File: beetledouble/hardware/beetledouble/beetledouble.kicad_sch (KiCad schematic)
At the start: 29 parts, among them J1 XT30PW-M, J2 rxin, J6 prog connector, U1 78L12G-AB3-R, U2 DD4012SB, U3 ATtiny1614-SS

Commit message: update pcb
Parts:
- added C?: 2.2uF 50V, Capacitor_SMD:C_0603_1608Metric, symbol Device:C
- added C?: 10uF 50V, Capacitor_SMD:C_1206_3216Metric, symbol Device:C
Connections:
- net +12V: now also C?.1, C?.1
- net GND: now also C?.2, C?.2
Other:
- moved on the sheet: C1, C2, TP1, U1

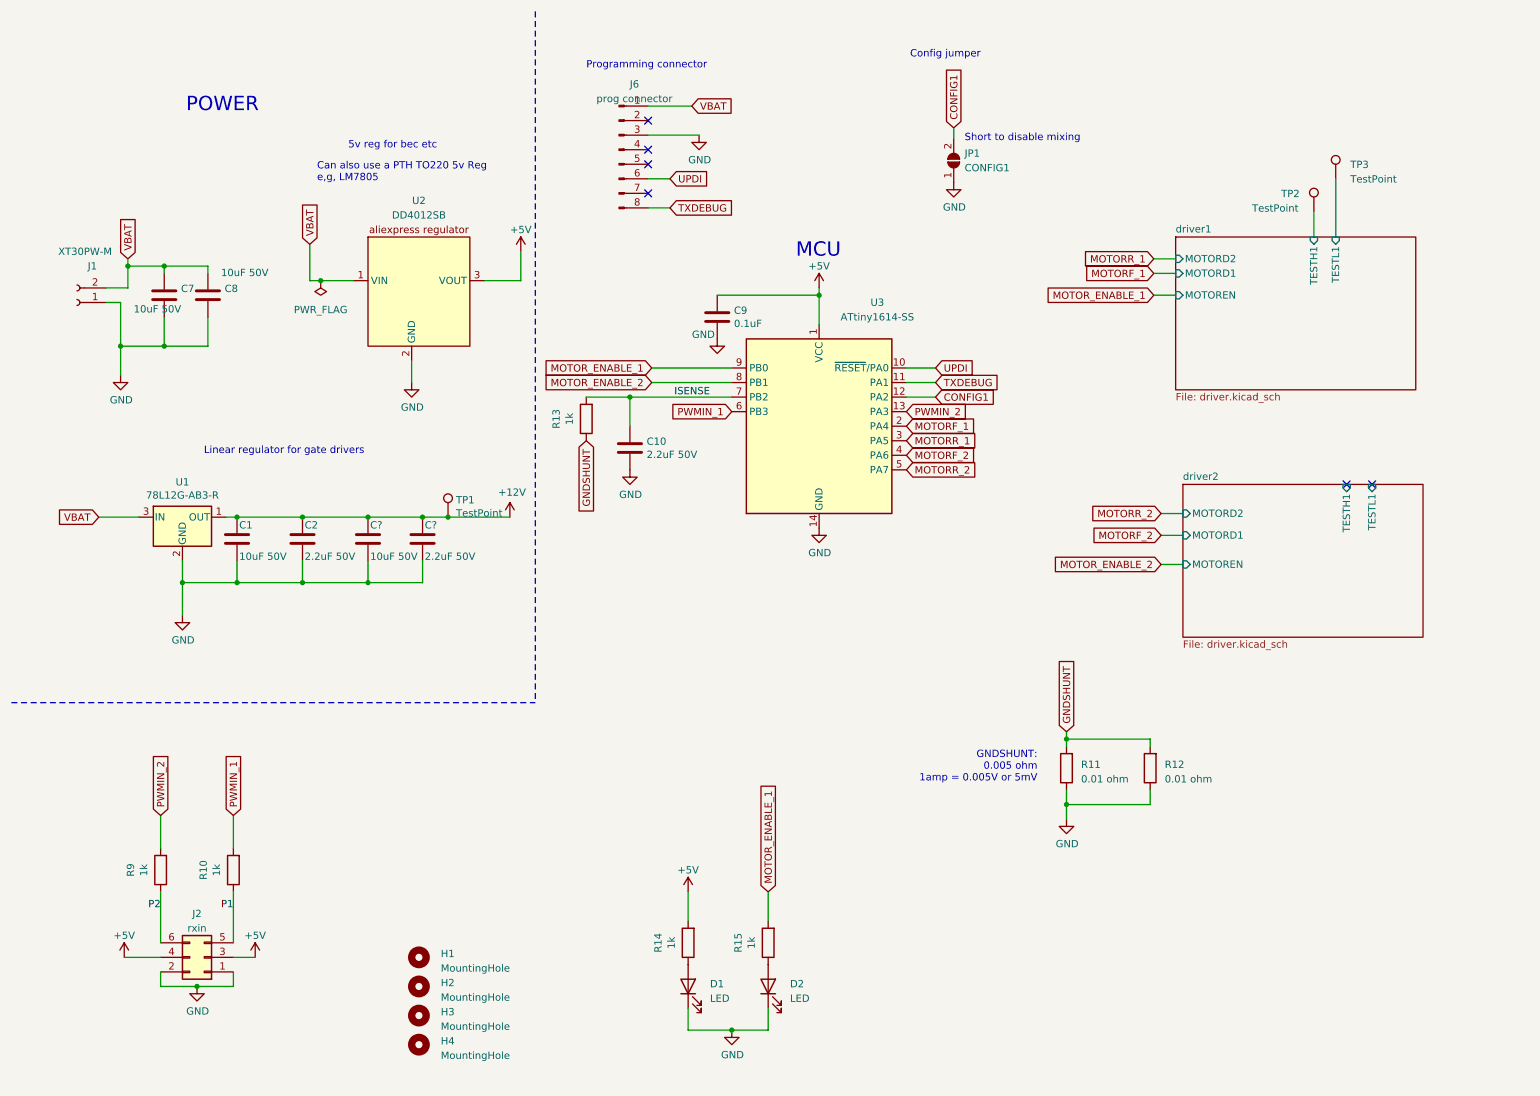
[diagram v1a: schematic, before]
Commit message: Minor pcb tweaks for better reliability solderability etc
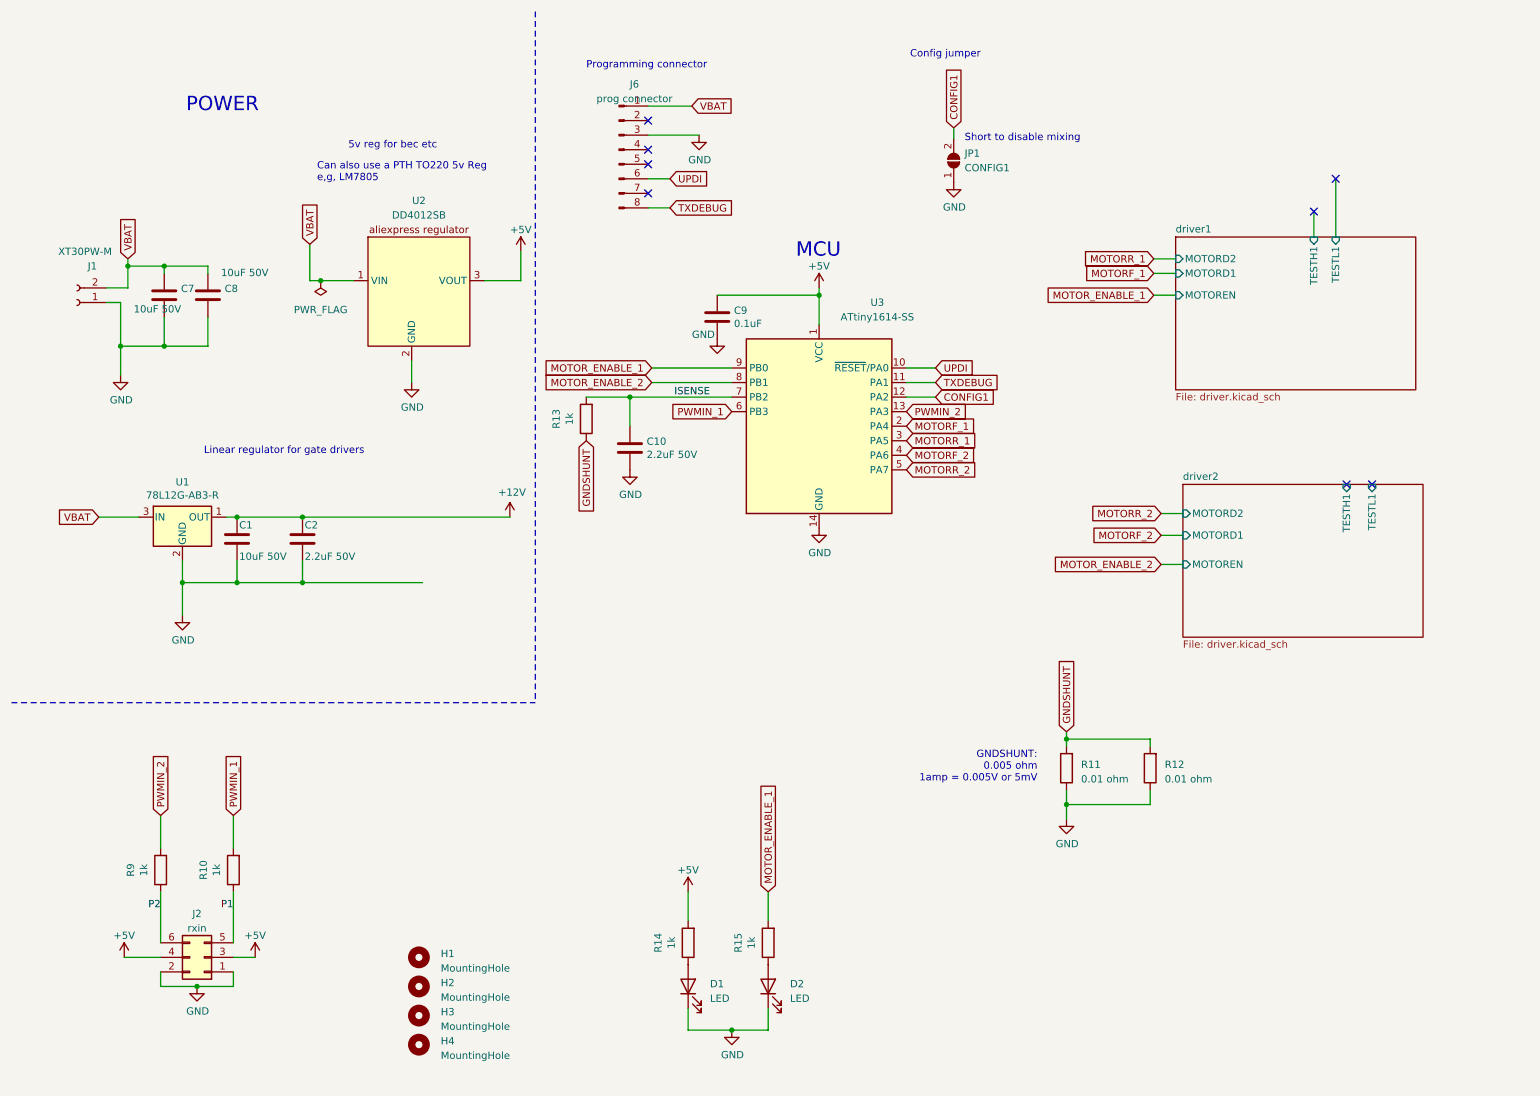
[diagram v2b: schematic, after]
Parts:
- removed C?: 2.2uF 50V, Capacitor_SMD:C_0603_1608Metric, symbol Device:C
- removed C?: 10uF 50V, Capacitor_SMD:C_1206_3216Metric, symbol Device:C
- removed TP1, TP2, TP3: TestPoint, TestPoint:TestPoint_Pad_1.5x1.5mm, symbol Connector:TestPoint
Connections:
- no-connect marks 6 -> 8
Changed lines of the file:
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@@
   (junction (at 62.23 111.125) (diameter 0) (color 0 0 0 0))
   (junction (at 65.405 58.42) (diameter 0.9144) (color 0 0 0 0))
-  (junction (at 73.66 99.695) (diameter 0) (color 0 0 0 0))
-  (junction (at 73.66 111.125) (diameter 0) (color 0 0 0 0))
-  (junction (at 83.185 99.695) (diameter 0) (color 0 0 0 0))
-  (junction (at 87.63 99.695) (diameter 0) (color 0 0 0 0))
   (junction (at 119.38 78.74) (diameter 0.9144) (color 0 0 0 0))
   (junction (at 137.16 189.23) (diameter 0.9144) (color 0 0 0 0))
@@
   (no_connect (at 122.555 38.1))
   (no_connect (at 122.555 43.18))
+  (no_connect (at 238.76 46.355))
+  (no_connect (at 242.57 40.64))
   (no_connect (at 244.475 93.98))
   (no_connect (at 248.92 93.98))
@@
     (stroke (width 0) (type default) (color 0 0 0 0))
   )
-  (wire (pts (xy 62.23 99.695) (xy 73.66 99.695))
+  (wire (pts (xy 62.23 99.695) (xy 98.425 99.695))
     (stroke (width 0) (type solid) (color 0 0 0 0))
   )
@@
     (stroke (width 0) (type default) (color 0 0 0 0))
   )
-  (wire (pts (xy 62.23 111.125) (xy 73.66 111.125))
+  (wire (pts (xy 62.23 111.125) (xy 83.185 111.125))
     (stroke (width 0) (type default) (color 0 0 0 0))
   )
@@
     (stroke (width 0) (type solid) (color 0 0 0 0))
   )
-  (wire (pts (xy 73.66 99.695) (xy 83.185 99.695))
-    (stroke (width 0) (type solid) (color 0 0 0 0))
-  )
-  (wire (pts (xy 73.66 107.315) (xy 73.66 111.125))
-    (stroke (width 0) (type solid) (color 0 0 0 0))
-  )
-  (wire (pts (xy 73.66 111.125) (xy 83.185 111.125))
-    (stroke (width 0) (type default) (color 0 0 0 0))
-  )
   (wire (pts (xy 81.28 72.39) (xy 81.28 76.2))
-    (stroke (width 0) (type solid) (color 0 0 0 0))
-  )
-  (wire (pts (xy 83.185 99.695) (xy 87.63 99.695))
-    (stroke (width 0) (type solid) (color 0 0 0 0))
-  )
-  (wire (pts (xy 83.185 107.315) (xy 83.185 111.125))
-    (stroke (width 0) (type default) (color 0 0 0 0))
-  )
-  (wire (pts (xy 87.63 99.695) (xy 98.425 99.695))
     (stroke (width 0) (type solid) (color 0 0 0 0))
   )
@@
     (pin "1")
   )
-  (symbol (lib_id "Connector:TestPoint") (at 87.63 99.695 0) (unit 1)
-    (in_bom yes) (on_board yes)
-    (property "Reference" "TP1" (id 0) (at 89.0271 96.7041 0)
-      (effects (font (size 1.27 1.27)) (justify left))
-    )
-    (property "Value" "TestPoint" (id 1) (at 89.0271 99.0028 0)
-      (effects (font (size 1.27 1.27)) (justify left))
-    )
-    (property "Footprint" "TestPoint:TestPoint_Pad_1.5x1.5mm" (id 2) (at 92.71 99.695 0)
-      (effects (font (size 1.27 1.27)) hide)
-    )
-    (property "Datasheet" "~" (id 3) (at 92.71 99.695 0)
-      (effects (font (size 1.27 1.27)) hide)
-    )
-    (pin "1")
-  )
-  (symbol (lib_id "Connector:TestPoint") (at 238.76 46.355 0) (unit 1)
-    (in_bom yes) (on_board yes)
-    (property "Reference" "TP2" (id 0) (at 233.045 43.2434 0)
-      (effects (font (size 1.27 1.27)) (justify left))
-    )
-    (property "Value" "TestPoint" (id 1) (at 227.965 45.7834 0)
-      (effects (font (size 1.27 1.27)) (justify left))
-    )
-    (property "Footprint" "TestPoint:TestPoint_Pad_1.5x1.5mm" (id 2) (at 243.84 46.355 0)
-      (effects (font (size 1.27 1.27)) hide)
-    )
-    (property "Datasheet" "~" (id 3) (at 243.84 46.355 0)
-      (effects (font (size 1.27 1.27)) hide)
-    )
-    (pin "1")
-  )
-  (symbol (lib_id "Connector:TestPoint") (at 242.57 40.64 0) (unit 1)
-    (in_bom yes) (on_board yes) (fields_autoplaced)
-    (property "Reference" "TP3" (id 0) (at 245.11 38.1634 0)
-      (effects (font (size 1.27 1.27)) (justify left))
-    )
-    (property "Value" "TestPoint" (id 1) (at 245.11 40.7034 0)
-      (effects (font (size 1.27 1.27)) (justify left))
-    )
-    (property "Footprint" "TestPoint:TestPoint_Pad_1.5x1.5mm" (id 2) (at 247.65 40.64 0)
-      (effects (font (size 1.27 1.27)) hide)
-    )
-    (property "Datasheet" "~" (id 3) (at 247.65 40.64 0)
-      (effects (font (size 1.27 1.27)) hide)
-    )
-    (pin "1")
-  )
   (symbol (lib_id "power:GND") (at 30.48 74.93 0) (unit 1)
     (in_bom yes) (on_board yes)
@@
     )
     (property "LCSC" "C162273" (id 4) (at 62.23 103.505 0)
-      (effects (font (size 1.27 1.27)) hide)
-    )
-    (pin "1")
-    (pin "2")
-  )
-  (symbol (lib_id "Device:C") (at 73.66 103.505 0) (unit 1)
-    (in_bom yes) (on_board yes)
-    (property "Reference" "C?" (id 0) (at 74.0411 101.0856 0)
-      (effects (font (size 1.27 1.27)) (justify left))
-    )
-    (property "Value" "10uF 50V" (id 1) (at 74.0411 106.5593 0)
-      (effects (font (size 1.27 1.27)) (justify left))
-    )
-    (property "Footprint" "Capacitor_SMD:C_1206_3216Metric" (id 2) (at 74.6252 107.315 0)
-      (effects (font (size 1.27 1.27)) hide)
-    )
-    (property "Datasheet" "~" (id 3) (at 73.66 103.505 0)
-      (effects (font (size 1.27 1.27)) hide)
-    )
-    (property "LCSC" "C13585" (id 4) (at 73.66 103.505 0)
-      (effects (font (size 1.27 1.27)) hide)
-    )
-    (pin "1")
-    (pin "2")
-  )
-  (symbol (lib_id "Device:C") (at 83.185 103.505 0) (unit 1)
-    (in_bom yes) (on_board yes)
-    (property "Reference" "C?" (id 0) (at 83.566 101.086 0)
-      (effects (font (size 1.27 1.27)) (justify left))
-    )
-    (property "Value" "2.2uF 50V" (id 1) (at 83.5661 106.5593 0)
-      (effects (font (size 1.27 1.27)) (justify left))
-    )
-    (property "Footprint" "Capacitor_SMD:C_0603_1608Metric" (id 2) (at 84.1502 107.315 0)
-      (effects (font (size 1.27 1.27)) hide)
-    )
-    (property "Datasheet" "~" (id 3) (at 83.185 103.505 0)
-      (effects (font (size 1.27 1.27)) hide)
-    )
-    (property "LCSC" "C162273" (id 4) (at 83.185 103.505 0)
       (effects (font (size 1.27 1.27)) hide)
     )
@@
     )
     (path "/04625774-148a-4b57-bc94-9367edc01ebb/349a753b-3547-4ca7-ac39-04fbb7832ae1"
-      (reference "C3") (unit 1) (value "2.2uF 50V") (footprint "Capacitor_SMD:C_0603_1608Metric")
+      (reference "C3") (unit 1) (value "4.7uF 50V") (footprint "Capacitor_SMD:C_0603_1608Metric_Pad1.08x0.95mm_HandSolder")
     )
     (path "/04625774-148a-4b57-bc94-9367edc01ebb/88333258-cec2-4c47-95fd-16fbcefc9469"
-      (reference "C4") (unit 1) (value "2.2uF 50V") (footprint "Capacitor_SMD:C_0603_1608Metric")
+      (reference "C4") (unit 1) (value "4.7uF 50V") (footprint "Capacitor_SMD:C_0603_1608Metric_Pad1.08x0.95mm_HandSolder")
     )
     (path "/4bcd2397-838c-4768-a766-b8196d1dcd9f/349a753b-3547-4ca7-ac39-04fbb7832ae1"
-      (reference "C5") (unit 1) (value "2.2uF 50V") (footprint "Capacitor_SMD:C_0603_1608Metric")
+      (reference "C5") (unit 1) (value "4.7uF 50V") (footprint "Capacitor_SMD:C_0603_1608Metric_Pad1.08x0.95mm_HandSolder")
     )
     (path "/4bcd2397-838c-4768-a766-b8196d1dcd9f/88333258-cec2-4c47-95fd-16fbcefc9469"
-      (reference "C6") (unit 1) (value "2.2uF 50V") (footprint "Capacitor_SMD:C_0603_1608Metric")
+      (reference "C6") (unit 1) (value "4.7uF 50V") (footprint "Capacitor_SMD:C_0603_1608Metric_Pad1.08x0.95mm_HandSolder")
     )
     (path "/c0d3d0e8-a176-42b6-b0cd-9761233332d3"
@@
       (reference "C18") (unit 1) (value "DNP") (footprint "Capacitor_SMD:C_1206_3216Metric")
     )
-    (path "/30343f26-46cc-4d31-b141-9bfb53fdd910"
-      (reference "C?") (unit 1) (value "2.2uF 50V") (footprint "Capacitor_SMD:C_0603_1608Metric")
-    )
-    (path "/8efccd41-0e97-49ce-828e-e46067ab6da1"
-      (reference "C?") (unit 1) (value "10uF 50V") (footprint "Capacitor_SMD:C_1206_3216Metric")
-    )
     (path "/c473e51e-eda3-4e25-b100-c0ce34b1e3be"
       (reference "D1") (unit 1) (value "LED") (footprint "LED_SMD:LED_0603_1608Metric_Pad1.05x0.95mm_HandSolder")
@@
       (reference "R15") (unit 1) (value "1k") (footprint "Resistor_SMD:R_0603_1608Metric")
     )
-    (path "/fc88e1ca-661b-4db6-9b7d-2eea0a896fbf"
-      (reference "TP1") (unit 1) (value "TestPoint") (footprint "TestPoint:TestPoint_Pad_1.5x1.5mm")
-    )
-    (path "/f5115f7a-1d77-4f8b-8d9e-bb3472f36bdc"
-      (reference "TP2") (unit 1) (value "TestPoint") (footprint "TestPoint:TestPoint_Pad_1.5x1.5mm")
-    )
-    (path "/587e4447-5d89-437b-993a-ea4091108cd4"
-      (reference "TP3") (unit 1) (value "TestPoint") (footprint "TestPoint:TestPoint_Pad_1.5x1.5mm")
-    )
     (path "/b612c31e-0d17-46e0-a098-3e7233416658"

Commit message: Hardware misc updates
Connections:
- net +5V: now also J6.1 (Pin_1)
- net VBAT: no longer J6.1 (Pin_1)
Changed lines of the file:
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@@
-    )
-  )
-  (global_label "VBAT" (shape input) (at 130.175 27.94 0)
-    (effects (font (size 1.27 1.27)) (justify left))
-    (property "Intersheet References" "${INTERSHEET_REFS}" (id 0) (at 138.5269 27.8606 0)
-      (effects (font (size 1.27 1.27)) (justify left) hide)
     )
   )
@@
     )
     (property "Datasheet" "" (id 3) (at 129.54 165.1 0)
+      (effects (font (size 1.27 1.27)) hide)
+    )
+    (pin "1")
+  )
+  (symbol (lib_id "power:+5V") (at 130.175 27.94 0) (unit 1)
+    (in_bom yes) (on_board yes) (fields_autoplaced)
+    (property "Reference" "#PWR?" (id 0) (at 130.175 31.75 0)
+      (effects (font (size 1.27 1.27)) hide)
+    )
+    (property "Value" "+5V" (id 1) (at 130.175 24.13 0))
+    (property "Footprint" "" (id 2) (at 130.175 27.94 0)
+      (effects (font (size 1.27 1.27)) hide)
+    )
+    (property "Datasheet" "" (id 3) (at 130.175 27.94 0)
       (effects (font (size 1.27 1.27)) hide)
     )
@@
       (reference "#PWR0103") (unit 1) (value "+5V") (footprint "")
     )
+    (path "/f49fba69-c05c-41e2-a90b-eea2537fb399"
+      (reference "#PWR?") (unit 1) (value "+5V") (footprint "")
+    )
     (path "/17b8893f-80ac-41c8-a26f-c0966dbbd091"
